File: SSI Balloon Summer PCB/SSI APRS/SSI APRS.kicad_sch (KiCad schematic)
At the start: 25 parts, among them J1 Conn_01x08, J4 APRS antenna, U12 TPS63070RNMR, U5 DRA818V

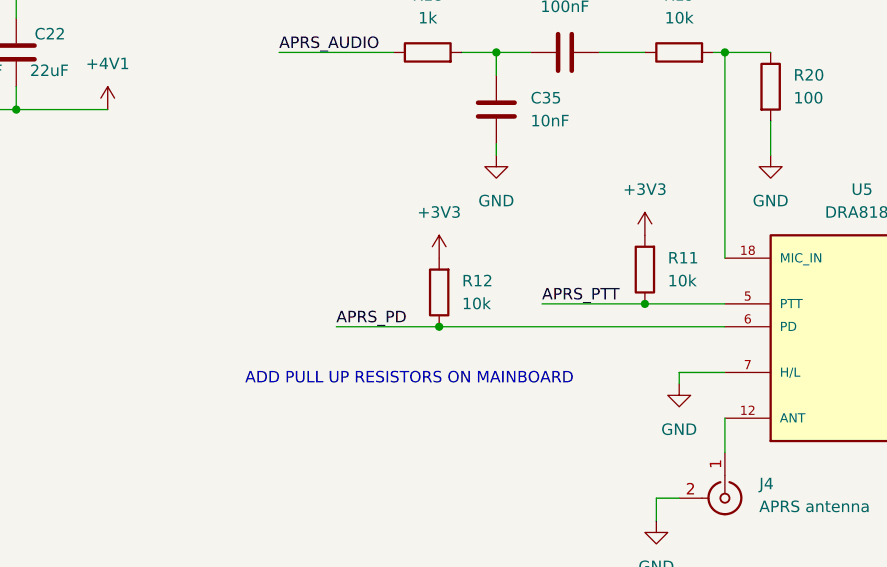
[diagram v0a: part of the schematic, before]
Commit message: Various rewiring: SWD, microSD, APRS JST
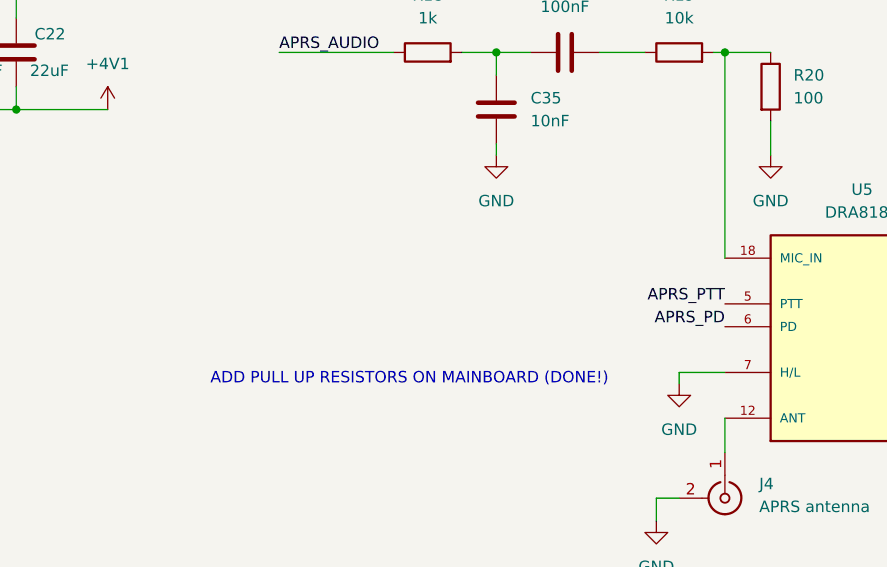
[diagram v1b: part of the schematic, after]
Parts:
- removed R11, R12: 10k, Resistor_SMD:R_0603_1608Metric, symbol Device:R
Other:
- note added: "ADD PULL UP RESISTORS ON MAINBOARD (DONE!)"
- note removed: "ADD PULL UP RESISTORS ON MAINBOARD"

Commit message: Cleaned APRS Filter up and adding Testing points
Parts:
- added R20B1: TBD, Resistor_SMD:R_0603_1608Metric, symbol Device:R
- added TP1, TP2, TP3, TP4, TP5, TP6, TP7: TestPoint, TestPoint:TestPoint_Pad_1.5x1.5mm, symbol Connector:TestPoint
- R20: value 100 -> 470
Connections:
- net +4V1: now also TP5.1
- net +5V: now also TP2.1
- net APRS_AUDIO: now also TP1.1
- net APRS_PD: now also TP6.1
- net APRS_PTT: now also TP7.1
- net GND: now also R20B1.2, TP3.1, TP4.1
- net at R19.2, R20.1, U5.18 (MIC_IN): now also R20B1.1

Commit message: Finished test points
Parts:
- renumbered TP5 to +4V1, TP2 to +5V_TEST1, TP1 to APRS_AUDIO1, TP6 to APRS_PD1, TP7 to APRS_PTT1, TP3 to GND1, TP4 to GND2
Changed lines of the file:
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@@
 		(dnp no)
 		(fields_autoplaced yes)
-		(property "Reference" "TP7"
+		(property "Reference" "APRS_PTT1"
 			(at 149.86 34.7979 0)
 			(show_name no)
@@
 			(project "SSI APRS"
 				(path "/6fdc2a63-d166-4024-986d-dc464eaf1c4d"
-					(reference "TP7")
+					(reference "APRS_PTT1")
 					(unit 1)
 				)
@@
 		(dnp no)
 		(fields_autoplaced yes)
-		(property "Reference" "TP4"
+		(property "Reference" "GND2"
 			(at 241.3 34.7979 0)
 			(show_name no)
@@
 			(project "SSI APRS"
 				(path "/6fdc2a63-d166-4024-986d-dc464eaf1c4d"
-					(reference "TP4")
+					(reference "GND2")
 					(unit 1)
 				)
@@
 		(dnp no)
 		(fields_autoplaced yes)
-		(property "Reference" "TP2"
+		(property "Reference" "+5V_TEST1"
 			(at 207.01 36.0679 0)
 			(show_name no)
@@
 			(project "SSI APRS"
 				(path "/6fdc2a63-d166-4024-986d-dc464eaf1c4d"
-					(reference "TP2")
+					(reference "+5V_TEST1")
 					(unit 1)
 				)
@@
 		(dnp no)
 		(fields_autoplaced yes)
-		(property "Reference" "TP6"
+		(property "Reference" "APRS_PD1"
 			(at 167.64 34.7979 0)
 			(show_name no)
@@
 			(project "SSI APRS"
 				(path "/6fdc2a63-d166-4024-986d-dc464eaf1c4d"
-					(reference "TP6")
+					(reference "APRS_PD1")
 					(unit 1)
 				)
@@
 		(dnp no)
 		(fields_autoplaced yes)
-		(property "Reference" "TP3"
+		(property "Reference" "GND1"
 			(at 223.52 34.7979 0)
 			(show_name no)
@@
 			(project "SSI APRS"
 				(path "/6fdc2a63-d166-4024-986d-dc464eaf1c4d"
-					(reference "TP3")
+					(reference "GND1")
 					(unit 1)
 				)
@@
 		(dnp no)
 		(fields_autoplaced yes)
-		(property "Reference" "TP5"
+		(property "Reference" "+4V1"
 			(at 256.54 34.7979 0)
 			(show_name no)
@@
 			(project "SSI APRS"
 				(path "/6fdc2a63-d166-4024-986d-dc464eaf1c4d"
-					(reference "TP5")
+					(reference "+4V1")
 					(unit 1)
 				)
@@
 		(dnp no)
 		(fields_autoplaced yes)
-		(property "Reference" "TP1"
+		(property "Reference" "APRS_AUDIO1"
 			(at 186.69 36.0679 0)
 			(show_name no)
@@
 			(project "SSI APRS"
 				(path "/6fdc2a63-d166-4024-986d-dc464eaf1c4d"
-					(reference "TP1")
+					(reference "APRS_AUDIO1")
 					(unit 1)
 				)

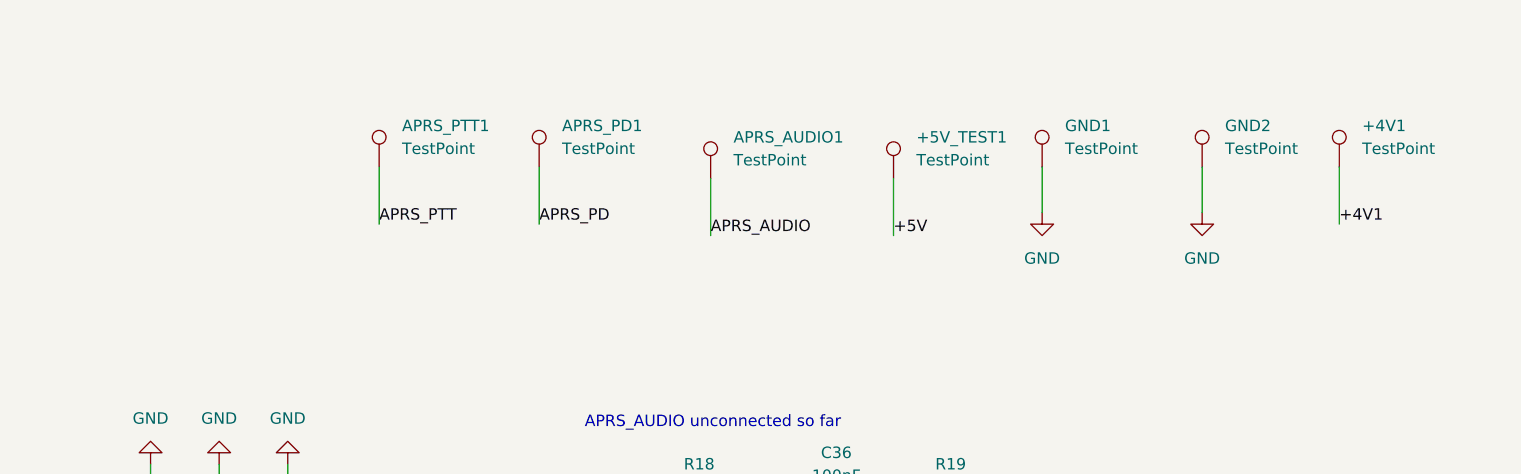
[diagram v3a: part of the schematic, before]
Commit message: Added Headers for testing, finalizing PCB
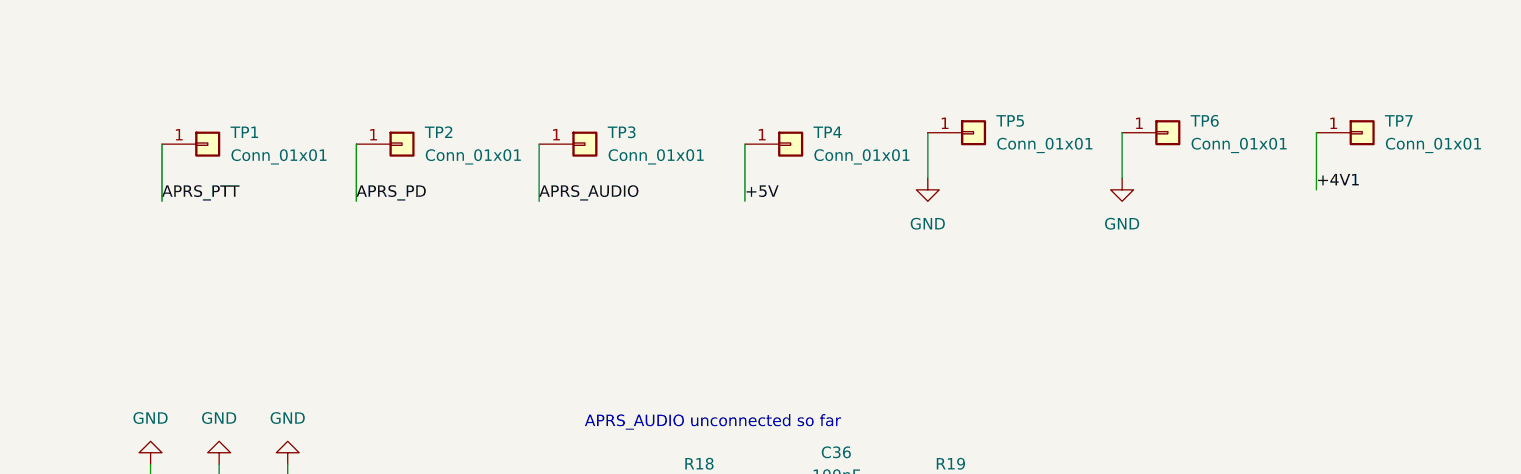
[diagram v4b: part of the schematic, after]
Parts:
- removed +4V1, +5V_TEST1, APRS_AUDIO1, APRS_PD1, APRS_PTT1, GND1, GND2: TestPoint, TestPoint:TestPoint_Pad_1.5x1.5mm, symbol Connector:TestPoint
- added TP1, TP2, TP3, TP4, TP5, TP6, TP7: Conn_01x01, Connector_PinHeader_2.54mm:PinHeader_1x01_P2.54mm_Vertical, symbol Connector_Generic:Conn_01x01
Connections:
- net +4V1: now also TP7.1 (Pin_1)
- net +5V: now also TP4.1 (Pin_1)
- net APRS_AUDIO: now also TP3.1 (Pin_1)
- net APRS_PD: now also TP2.1 (Pin_1)
- net APRS_PTT: now also TP1.1 (Pin_1)
- net GND: now also TP5.1 (Pin_1), TP6.1 (Pin_1)

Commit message: Updated antenna connector
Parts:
- J4: footprint Connector_Coaxial:U.FL_Hirose_U.FL-R-SMT-1_Vertical -> Connector_Coaxial:SMA_Amphenol_901-144_Vertical
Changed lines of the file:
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@@
 			)
 		)
-		(property "Footprint" "Connector_Coaxial:U.FL_Hirose_U.FL-R-SMT-1_Vertical"
+		(property "Footprint" "Connector_Coaxial:SMA_Amphenol_901-144_Vertical"
 			(at 215.9 128.27 0)
 			(hide yes)

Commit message: BOM for APRS board done - motherboard next
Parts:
- C15, C16, C23: LCSC (none) -> C5189822
- C17, C18: LCSC (none) -> C237435
- C19: value 100 nF -> 100nF; LCSC (none) -> C519438
- C20, C21, C22: LCSC (none) -> C907991
- C35: LCSC (none) -> C3836718
- C36, C37: LCSC (none) -> C519438
- J1: LCSC (none) -> C5306549
- J4: LCSC (none) -> C376663
- L2: LCSC (none) -> C18547833
- R10: value 100k -> 120k; LCSC (none) -> C25808
- R18: LCSC (none) -> C21190
- R19, R7: LCSC (none) -> C25804
- R20: LCSC (none) -> C23179
- R9: value 412k -> 510k; LCSC (none) -> C23192
- TP1, TP2, TP3, TP4, TP5, TP6, TP7: LCSC (none) -> C81276
- U12: LCSC (none) -> C109322

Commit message: finished finding all parts on JLCPCB - finalizing BOM then order
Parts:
- C15, C16, C23: LCSC C5189822 -> C92009
- C17, C18: LCSC C237435 -> C344022
- C20, C21, C22: LCSC C907991 -> C48986262
- J1: LCSC C5306549 -> C157914
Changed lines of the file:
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@@
 			)
 		)
-		(property "LCSC" "C907991"
+		(property "LCSC" "C48986262"
 			(at 121.92 78.74 0)
 			(hide yes)
@@
 			)
 		)
-		(property "LCSC" "C907991"
+		(property "LCSC" "C48986262"
 			(at 129.54 78.74 0)
 			(hide yes)
@@
 			)
 		)
-		(property "LCSC" "C5189822"
+		(property "LCSC" "C92009"
 			(at 257.81 93.98 0)
 			(hide yes)
@@
 			)
 		)
-		(property "LCSC" "C5306549"
+		(property "LCSC" "C157914"
 			(at 45.72 40.64 0)
 			(hide yes)
@@
 			)
 		)
-		(property "LCSC" "C237435"
+		(property "LCSC" "C344022"
 			(at 99.06 78.74 0)
 			(hide yes)
@@
 			)
 		)
-		(property "LCSC" "C237435"
+		(property "LCSC" "C344022"
 			(at 57.15 78.74 0)
 			(hide yes)
@@
 			)
 		)
-		(property "LCSC" "C907991"
+		(property "LCSC" "C48986262"
 			(at 137.16 78.74 0)
 			(hide yes)
@@
 			)
 		)
-		(property "LCSC" "C5189822"
+		(property "LCSC" "C92009"
 			(at 39.37 78.74 0)
 			(hide yes)
@@
 			)
 		)
-		(property "LCSC" "C5189822"
+		(property "LCSC" "C92009"
 			(at 31.75 78.74 0)
 			(hide yes)

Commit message: PCB finally done i think and ready to order
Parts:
- C15, C16, C23: LCSC C92009 -> C15850
- C19, C36, C37: LCSC C519438 -> C14663
- U5: now left out of the parts list
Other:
- note removed: "ADD PULL UP RESISTORS ON MAINBOARD (DONE!)"
- note removed: "APRS_AUDIO unconnected so far"
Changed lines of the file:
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@@
 		)
 	)
-	(text "APRS_AUDIO unconnected so far"
-		(exclude_from_sim no)
-		(at 184.404 67.818 0)
-		(effects
-			(font
-				(size 1.27 1.27)
-			)
-		)
-	)
-	(text "ADD PULL UP RESISTORS ON MAINBOARD (DONE!)"
-		(exclude_from_sim no)
-		(at 180.848 115.062 0)
-		(effects
-			(font
-				(size 1.27 1.27)
-			)
-		)
-	)
 	(junction
 		(at 43.18 85.09)
@@
 			)
 		)
-		(property "LCSC" "C519438"
+		(property "LCSC" "C14663"
 			(at 248.92 93.98 0)
 			(hide yes)
@@
 			)
 		)
-		(property "LCSC" "C519438"
+		(property "LCSC" "C14663"
 			(at 198.12 78.74 90)
 			(hide yes)
@@
 			)
 		)
-		(property "LCSC" "C92009"
+		(property "LCSC" "C15850"
 			(at 257.81 93.98 0)
 			(hide yes)
@@
 		(body_style 1)
 		(exclude_from_sim no)
-		(in_bom yes)
+		(in_bom no)
 		(on_board yes)
 		(in_pos_files yes)
@@
 			)
 		)
-		(property "LCSC" "C92009"
+		(property "LCSC" "C15850"
 			(at 39.37 78.74 0)
 			(hide yes)
@@
 			)
 		)
-		(property "LCSC" "C519438"
+		(property "LCSC" "C14663"
 			(at 106.68 105.41 90)
 			(hide yes)
@@
 			)
 		)
-		(property "LCSC" "C92009"
+		(property "LCSC" "C15850"
 			(at 31.75 78.74 0)
 			(hide yes)
